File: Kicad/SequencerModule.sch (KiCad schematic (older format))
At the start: 13 parts, among them U1 L78L05_SOT89, U2 MCP4822, U4 TL072

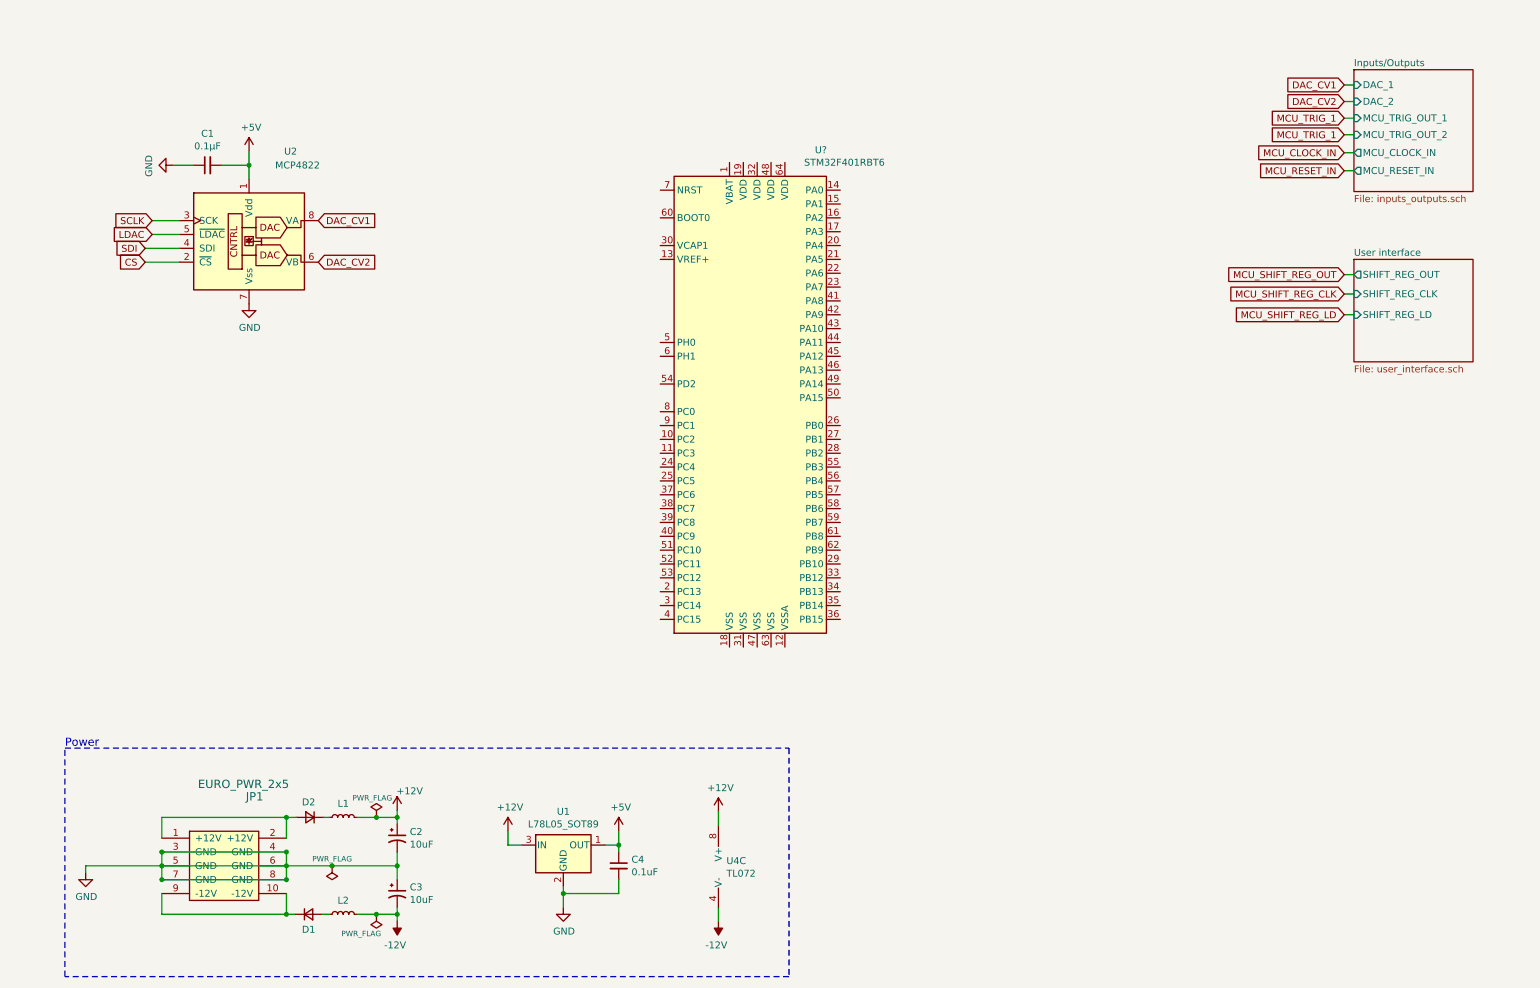
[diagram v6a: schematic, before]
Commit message: updated power section with switching regulator
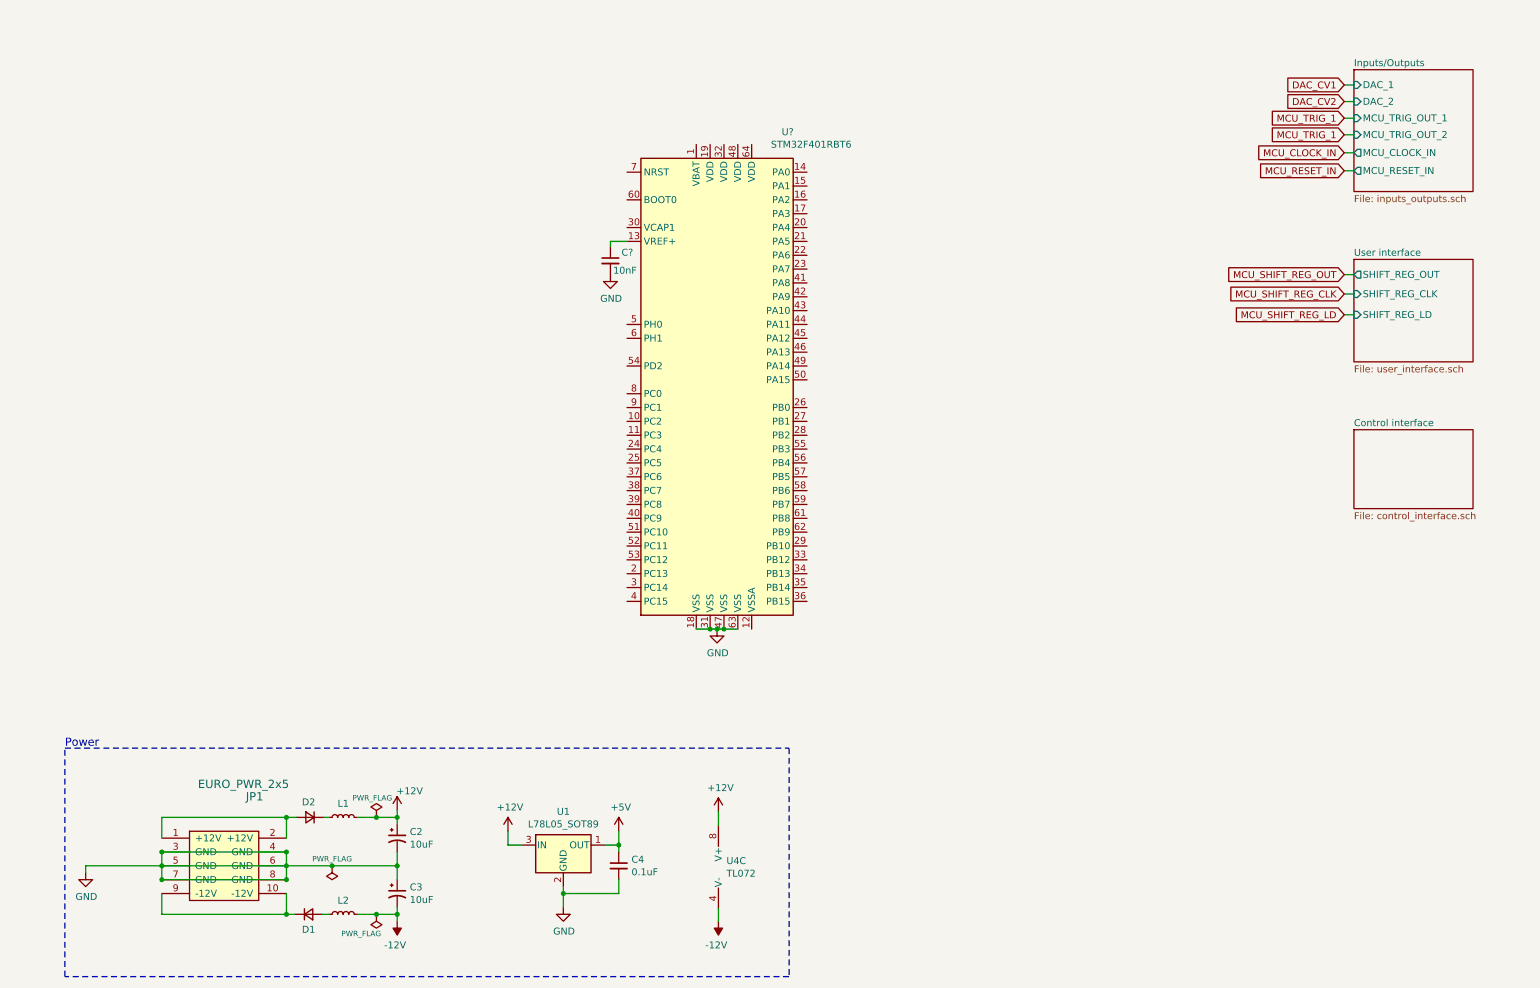
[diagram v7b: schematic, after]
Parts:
- removed C1: 0.1μF, symbol Device:C_Small
- removed U2: MCP4822, symbol Analog_DAC:MCP4822
- added C?: 10nF, symbol Device:C_Small
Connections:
- net GND: now also U?.18 (VSS), U?.31 (VSS), U?.47 (VSS), U?.63 (VSS), C?.2
- net at U?.13 (VREF+): now also C?.1
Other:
- moved on the sheet: U?
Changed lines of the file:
@@
 $Descr A4 11693 8268
 encoding utf-8
-Sheet 1 3
+Sheet 1 4
 Title "Eurorack sequencer module"
 Date "2020-11-30"
@@
 $EndSheet
 $Comp
-L Analog_DAC:MCP4822 U2
-U 1 1 5FAC40C6
-P 2180 2190
-F 0 "U2" H 2480 2790 50  0000 C CNN
-F 1 "MCP4822" H 2530 2690 50  0000 C CNN
-F 2 "" H 2980 1890 50  0001 C CNN
-F 3 "http://ww1.microchip.com/downloads/en/DeviceDoc/20002249B.pdf" H 2980 1890 50  0001 C CNN
-	1    2180 2190
-	1    0    0    -1
-$EndComp
-$Comp
-L power:GND #PWR0101
-U 1 1 5FAC5967
-P 2180 2690
-F 0 "#PWR0101" H 2180 2440 50  0001 C CNN
-F 1 "GND" H 2185 2517 50  0000 C CNN
-F 2 "" H 2180 2690 50  0001 C CNN
-F 3 "" H 2180 2690 50  0001 C CNN
-	1    2180 2690
-	1    0    0    -1
-$EndComp
-$Comp
-L Device:C_Small C1
-U 1 1 5FAC8AF5
-P 1880 1690
-F 0 "C1" V 2109 1690 50  0000 C CNN
-F 1 "0.1μF" V 2018 1690 50  0000 C CNN
-F 2 "" H 1880 1690 50  0001 C CNN
-F 3 "~" H 1880 1690 50  0001 C CNN
-	1    1880 1690
-	0    -1   -1   0
-$EndComp
-Wire Wire Line
-	2180 1590 2180 1690
-Wire Wire Line
-	1980 1690 2180 1690
-Connection ~ 2180 1690
-Wire Wire Line
-	2180 1690 2180 1790
-$Comp
-L power:GND #PWR0102
-U 1 1 5FAC9D1B
-P 1630 1690
-F 0 "#PWR0102" H 1630 1440 50  0001 C CNN
-F 1 "GND" H 1635 1517 50  0000 C CNN
-F 2 "" H 1630 1690 50  0001 C CNN
-F 3 "" H 1630 1690 50  0001 C CNN
-	1    1630 1690
-	0    1    1    0
-$EndComp
-Wire Wire Line
-	1630 1690 1780 1690
-Text GLabel 1480 2090 0    50   Input ~ 0
-SCLK
-Text GLabel 1430 2390 0    50   Input ~ 0
-CS
-Text GLabel 2680 2090 2    50   Input ~ 0
-DAC_CV1
-Text GLabel 2680 2390 2    50   Input ~ 0
-DAC_CV2
-Wire Wire Line
-	1480 2090 1680 2090
-Wire Wire Line
-	1480 2190 1680 2190
-Wire Wire Line
-	1430 2290 1680 2290
-Wire Wire Line
-	1430 2390 1680 2390
-Text GLabel 1430 2290 0    50   Input ~ 0
-SDI
-$Comp
 L Device:D_Small D2
 U 1 1 5FB17EBE
@@
 	4850 6500 4850 6600
 Connection ~ 4850 6600
-$Comp
-L power:+5V #PWR0110
-U 1 1 5FB4B6EF
-P 2180 1590
-F 0 "#PWR0110" H 2180 1440 50  0001 C CNN
-F 1 "+5V" H 2195 1763 50  0000 C CNN
-F 2 "" H 2180 1590 50  0001 C CNN
-F 3 "" H 2180 1590 50  0001 C CNN
-	1    2180 1590
-	1    0    0    -1
-$EndComp
 $Comp
 L eurorack_custom:urorack_EURO_PWR_2x5 JP1
@@
 Wire Wire Line
 	10090 2770 10160 2770
-Text GLabel 1480 2190 0    50   Input ~ 0
-LDAC
 $Comp
 L power:PWR_FLAG #FLG0101
@@
 L MCU_ST_STM32F4:STM32F401RBTx U?
 U 1 1 5FCBFD96
-P 5850 3370
-F 0 "U?" H 6310 5160 50  0000 C CNN
-F 1 "STM32F401RBT6" H 6480 5070 50  0000 C CNN
-F 2 "Package_QFP:LQFP-64_10x10mm_P0.5mm" H 5250 1670 50  0001 R CNN
-F 3 "http://www.st.com/st-web-ui/static/active/en/resource/technical/document/datasheet/DM00086815.pdf" H 5850 3370 50  0001 C CNN
-	1    5850 3370
-	1    0    0    -1
-$EndComp
+P 5610 3240
+F 0 "U?" H 6070 5030 50  0000 C CNN
+F 1 "STM32F401RBT6" H 6240 4940 50  0000 C CNN
+F 2 "Package_QFP:LQFP-64_10x10mm_P0.5mm" H 5010 1540 50  0001 R CNN
+F 3 "http://www.st.com/st-web-ui/static/active/en/resource/technical/document/datasheet/DM00086815.pdf" H 5610 3240 50  0001 C CNN
+	1    5610 3240
+	1    0    0    -1
+$EndComp
+$Sheet
+S 10160 3600 860  570
+U 5FE50EBA
+F0 "Control interface" 50
+F1 "control_interface.sch" 50
+$EndSheet
+$Comp
+L power:GND #PWR?
+U 1 1 5FD65173
+P 5560 5040
+F 0 "#PWR?" H 5560 4790 50  0001 C CNN
+F 1 "GND" H 5565 4867 50  0000 C CNN
+F 2 "" H 5560 5040 50  0001 C CNN
+F 3 "" H 5560 5040 50  0001 C CNN
+	1    5560 5040
+	1    0    0    -1
+$EndComp
+Wire Wire Line
+	5410 5040 5510 5040
+Connection ~ 5510 5040
+Wire Wire Line
+	5510 5040 5560 5040
+Connection ~ 5610 5040
+Wire Wire Line
+	5610 5040 5710 5040
+Connection ~ 5560 5040
+Wire Wire Line
+	5560 5040 5610 5040
+$Comp
+L Device:C_Small C?
+U 1 1 5FD67219
+P 4790 2380
+F 0 "C?" H 4870 2440 50  0000 L CNN
+F 1 "10nF" H 4810 2310 50  0000 L CNN
+F 2 "" H 4790 2380 50  0001 C CNN
+F 3 "~" H 4790 2380 50  0001 C CNN
+	1    4790 2380
+	1    0    0    -1
+$EndComp
+Wire Wire Line
+	4790 2280 4790 2240
+Wire Wire Line
+	4790 2240 4910 2240
+$Comp
+L power:GND #PWR?
+U 1 1 5FD68F2E
+P 4790 2480
+F 0 "#PWR?" H 4790 2230 50  0001 C CNN
+F 1 "GND" H 4795 2307 50  0000 C CNN
+F 2 "" H 4790 2480 50  0001 C CNN
+F 3 "" H 4790 2480 50  0001 C CNN
+	1    4790 2480
+	1    0    0    -1
+$EndComp
